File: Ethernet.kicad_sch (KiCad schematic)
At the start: 34 parts, among them J8 RJ45_Abracon_ARJP11A-MASA-B-A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, U4 LAN8742A-CZ-TR, U5 USBLC6-4SC6, Y2 25M

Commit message: cleaner, still needs full checklisting
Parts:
- J8: footprint Connector_RJ:RJ45_Abracon_ARJP11A-MA_Horizontal -> UTSVT_Connectors:RJ45_Abracon_ARJP11A-MA_Horizontal
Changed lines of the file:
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@@
       (effects (font (size 1.27 1.27)))
     )
-    (property "Footprint" "Connector_RJ:RJ45_Abracon_ARJP11A-MA_Horizontal" (at 251.46 125.73 0)
+    (property "Footprint" "UTSVT_Connectors:RJ45_Abracon_ARJP11A-MA_Horizontal" (at 251.46 125.73 0)
       (effects (font (size 1.27 1.27)) hide)
     )

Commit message: bom, gerbers, edge cuts, footprint verification
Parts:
- C24, C25: P/N (none) -> 08051A300JAT2A
- C26: P/N (none) -> 08055A471FAT4A
- C27: P/N (none) -> 08055C105K4T4A
- C28, C29, C30, C31, C33, C34: P/N (none) -> C0805C104K5RAC7411
- C32: P/N (none) -> T491A106K016AT
- J8: P/N (none) -> ARJP11A-MASA-B-A-EMU2
- R10, R11, R6, R7, R9: P/N (none) -> CRCW080533R0JNEA
- R12, R13, R15, R16, R8: P/N (none) -> CRCW080510K0FKEAC
- R14: P/N (none) -> CRCW080521K5FKEA
- R17, R19, R20, R21: P/N (none) -> CRCW080550R0FKTA
- R18: P/N (none) -> CRCW080512K1FKEA
- R22, R23: P/N (none) -> CRCW0805120RFKEAC
- U4: P/N (none) -> LAN8742A-CZ-TR
- U5: P/N (none) -> USBLC6-4SC6
- Y2: P/N (none) -> FOXSDLF/250F-20
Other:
- note added: "Load capacitance of ~20p"

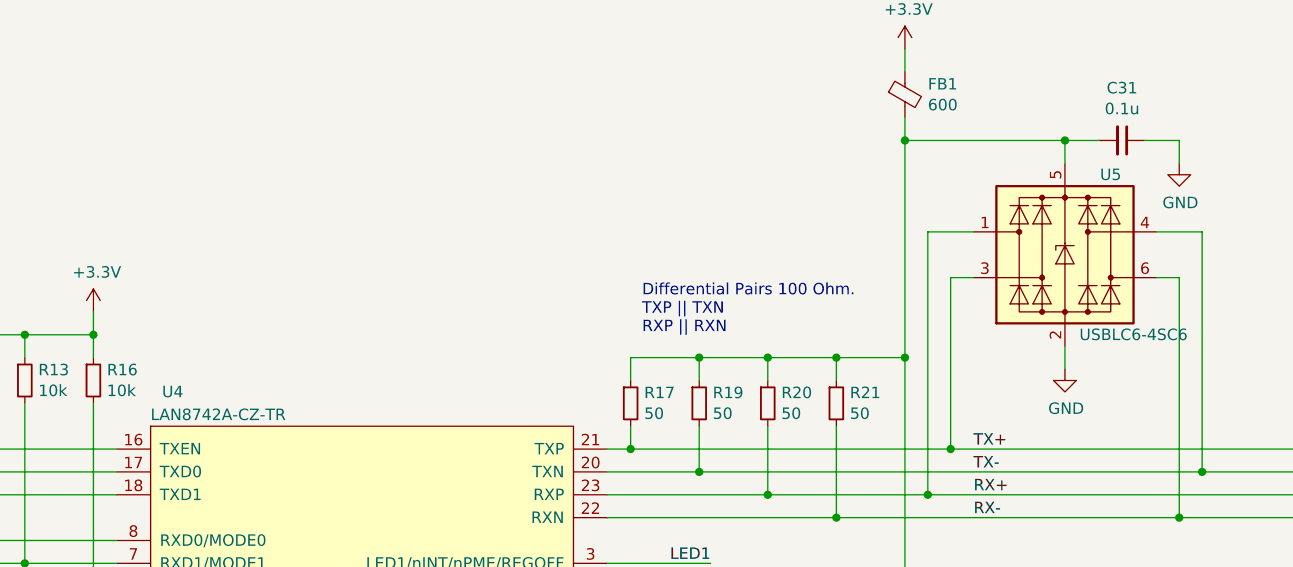
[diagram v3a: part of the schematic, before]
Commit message: bluetooth schematic additions
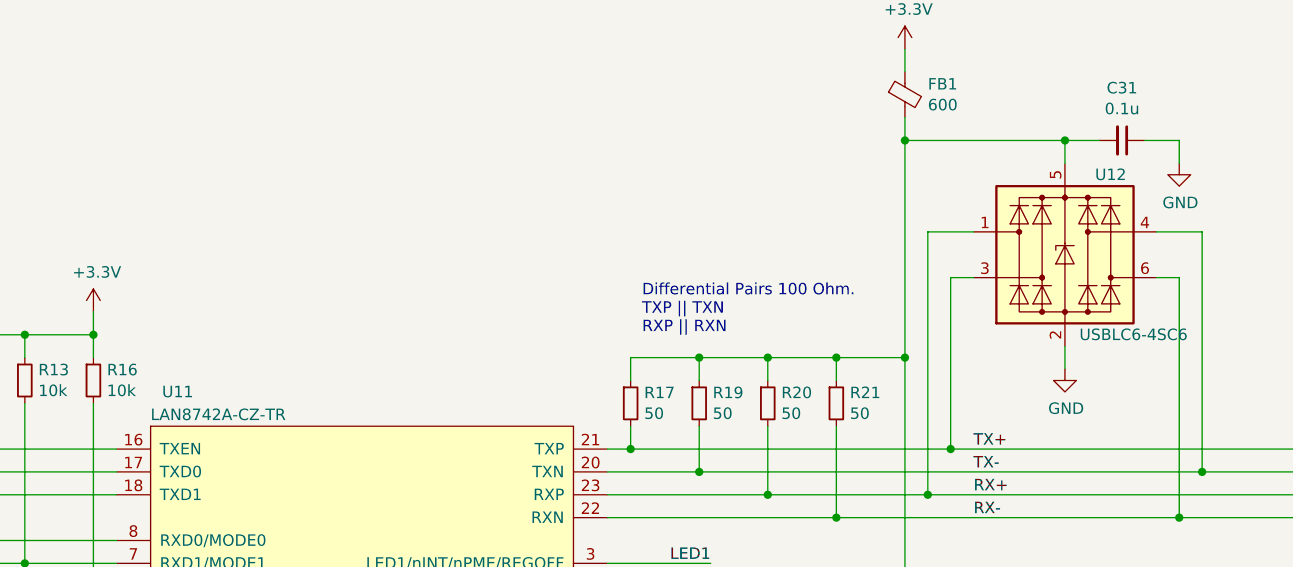
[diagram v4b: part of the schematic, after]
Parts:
- renumbered U4 to U11, U5 to U12
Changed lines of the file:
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@@
   (symbol (lib_id "Power_Protection:USBLC6-4SC6") (at 180.34 63.5 0) (unit 1)
     (in_bom yes) (on_board yes) (dnp no)
-    (property "Reference" "U5" (at 185.42 54.61 0)
+    (property "Reference" "U12" (at 185.42 54.61 0)
       (effects (font (size 1.27 1.27)))
     )
@@
       (project "Telemetry-Primary"
         (path "/7f2a449b-14af-42b3-8d38-5f0f8a5ee7ce/00000000-0000-0000-0000-00005f716da6"
-          (reference "U5") (unit 1)
+          (reference "U12") (unit 1)
         )
       )
@@
   (symbol (lib_id "utsvt-chips:LAN8742A-CZ-TR") (at 96.52 82.55 0) (unit 1)
     (in_bom yes) (on_board yes) (dnp no)
-    (property "Reference" "U4" (at 80.01 78.74 0)
+    (property "Reference" "U11" (at 80.01 78.74 0)
       (effects (font (size 1.27 1.27)) (justify left))
     )
@@
       (project "Telemetry-Primary"
         (path "/7f2a449b-14af-42b3-8d38-5f0f8a5ee7ce/00000000-0000-0000-0000-00005f716da6"
-          (reference "U4") (unit 1)
+          (reference "U11") (unit 1)
         )
       )

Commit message: new bt module + preliminary reverse protection
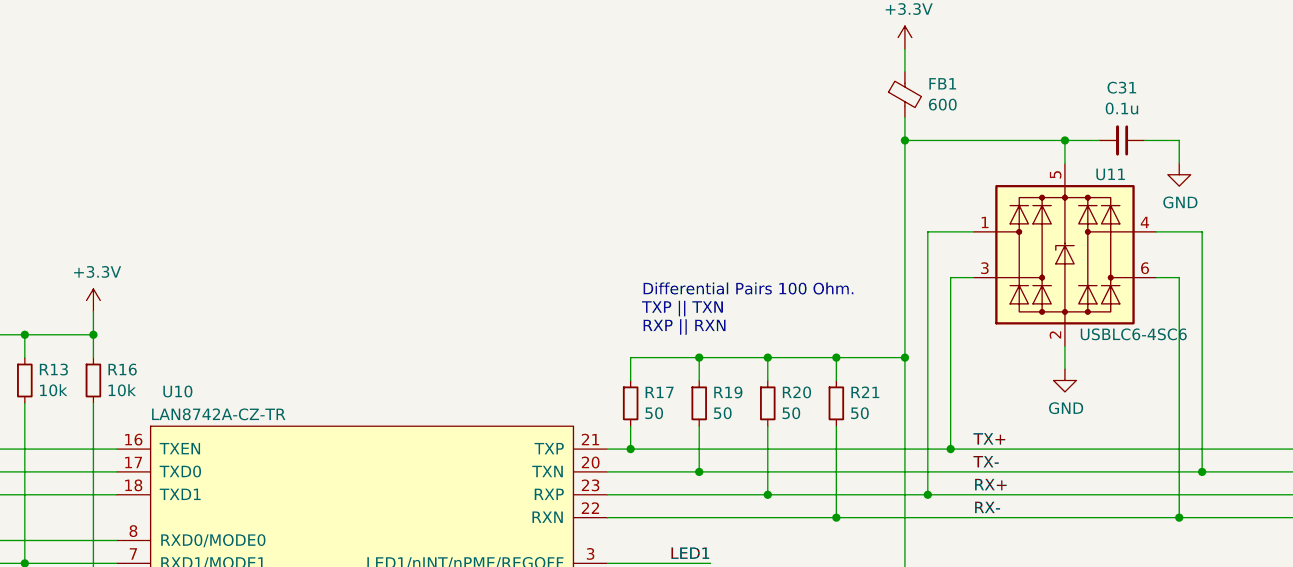
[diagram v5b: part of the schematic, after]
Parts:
- renumbered U11 to U10, U12 to U11
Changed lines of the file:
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@@
   (symbol (lib_id "Power_Protection:USBLC6-4SC6") (at 180.34 63.5 0) (unit 1)
     (in_bom yes) (on_board yes) (dnp no)
-    (property "Reference" "U12" (at 185.42 54.61 0)
+    (property "Reference" "U11" (at 185.42 54.61 0)
       (effects (font (size 1.27 1.27)))
     )
@@
       (project "Telemetry-Primary"
         (path "/7f2a449b-14af-42b3-8d38-5f0f8a5ee7ce/00000000-0000-0000-0000-00005f716da6"
-          (reference "U12") (unit 1)
+          (reference "U11") (unit 1)
         )
       )
@@
   (symbol (lib_id "utsvt-chips:LAN8742A-CZ-TR") (at 96.52 82.55 0) (unit 1)
     (in_bom yes) (on_board yes) (dnp no)
-    (property "Reference" "U11" (at 80.01 78.74 0)
+    (property "Reference" "U10" (at 80.01 78.74 0)
       (effects (font (size 1.27 1.27)) (justify left))
     )
@@
       (project "Telemetry-Primary"
         (path "/7f2a449b-14af-42b3-8d38-5f0f8a5ee7ce/00000000-0000-0000-0000-00005f716da6"
-          (reference "U11") (unit 1)
+          (reference "U10") (unit 1)
         )
       )

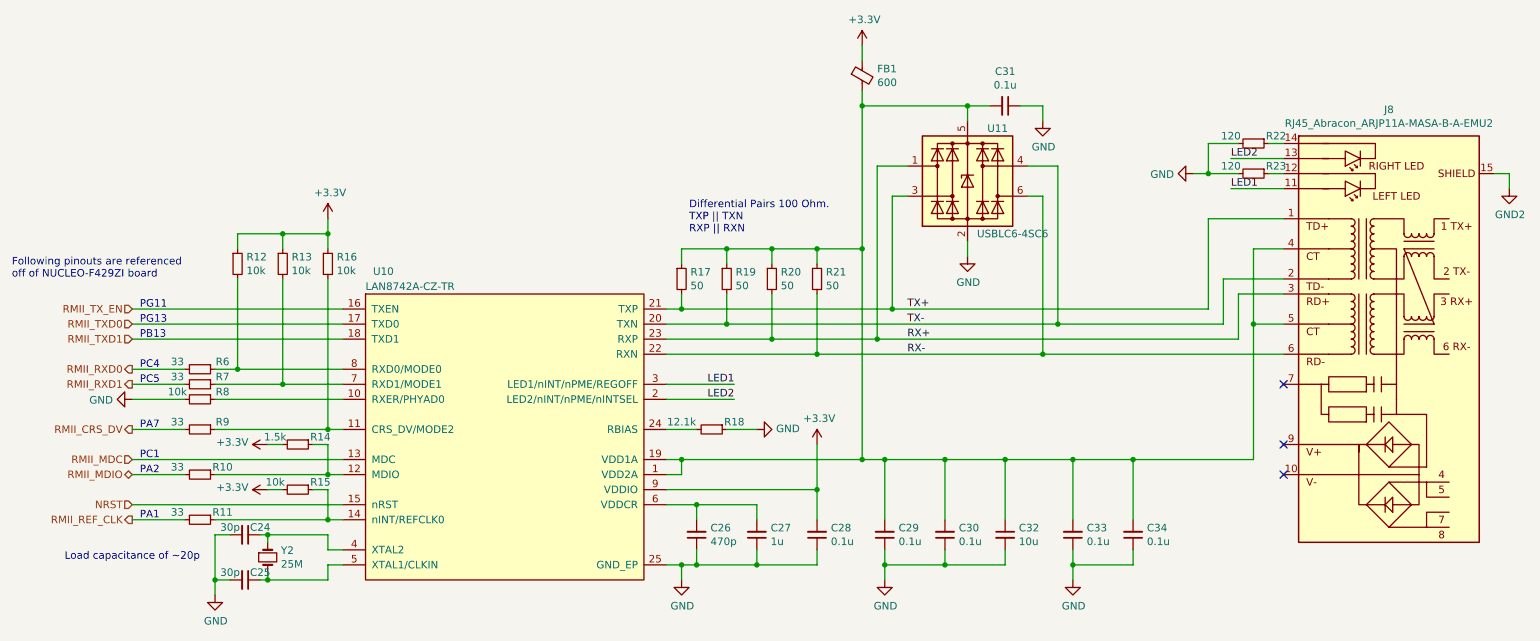
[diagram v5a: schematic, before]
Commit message: inputs routing + fixed models + clock keepouts
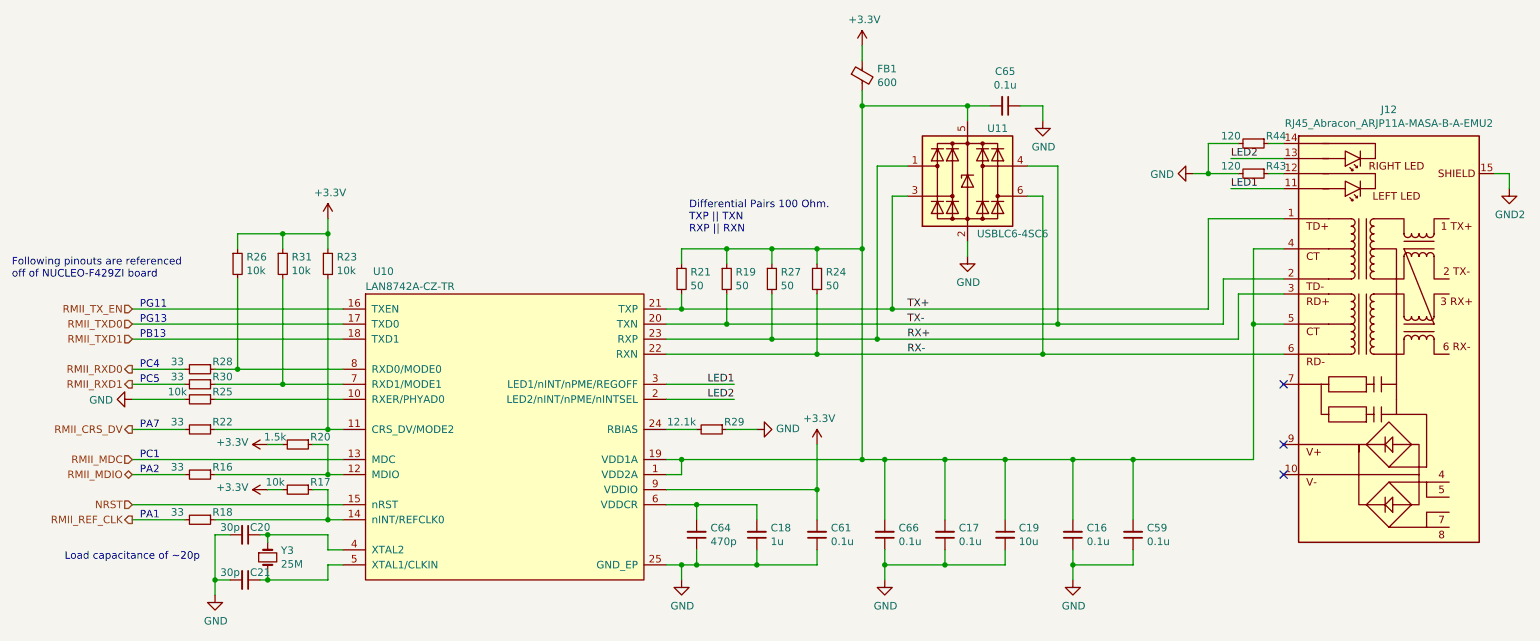
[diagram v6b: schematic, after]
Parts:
- renumbered C33 to C16, C30 to C17, C27 to C18, C32 to C19, C24 to C20, C25 to C21, C34 to C59, C28 to C61, C26 to C64, C31 to C65, C29 to C66, J8 to J12, R10 to R16, R15 to R17, R11 to R18, R14 to R20, R17 to R21, R9 to R22, R16 to R23, R21 to R24, R8 to R25, R12 to R26, R20 to R27, R6 to R28, R18 to R29, R7 to R30, R13 to R31, R23 to R43, R22 to R44, Y2 to Y3
